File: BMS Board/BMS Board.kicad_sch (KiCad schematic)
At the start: 22 parts

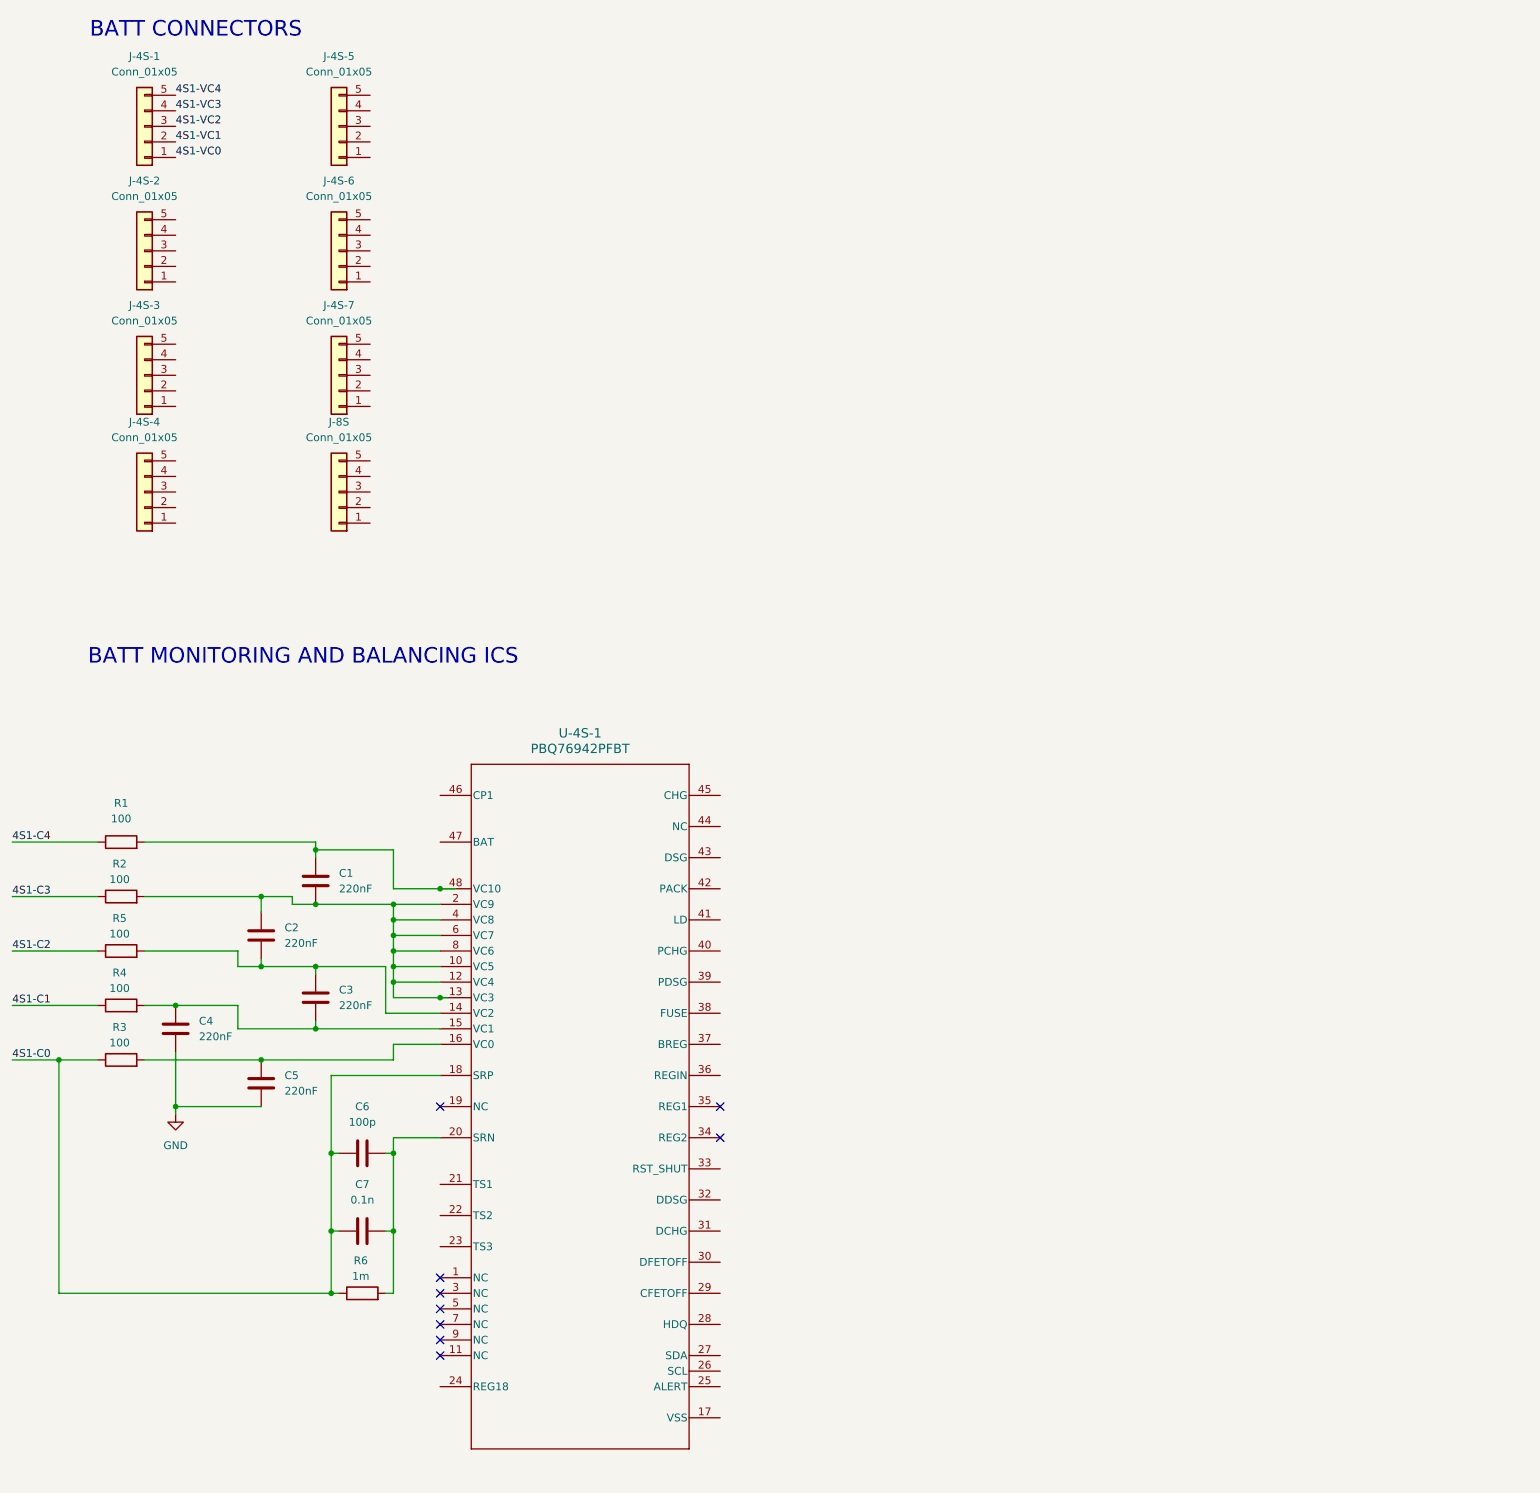
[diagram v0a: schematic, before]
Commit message: more pin configs for bq chip
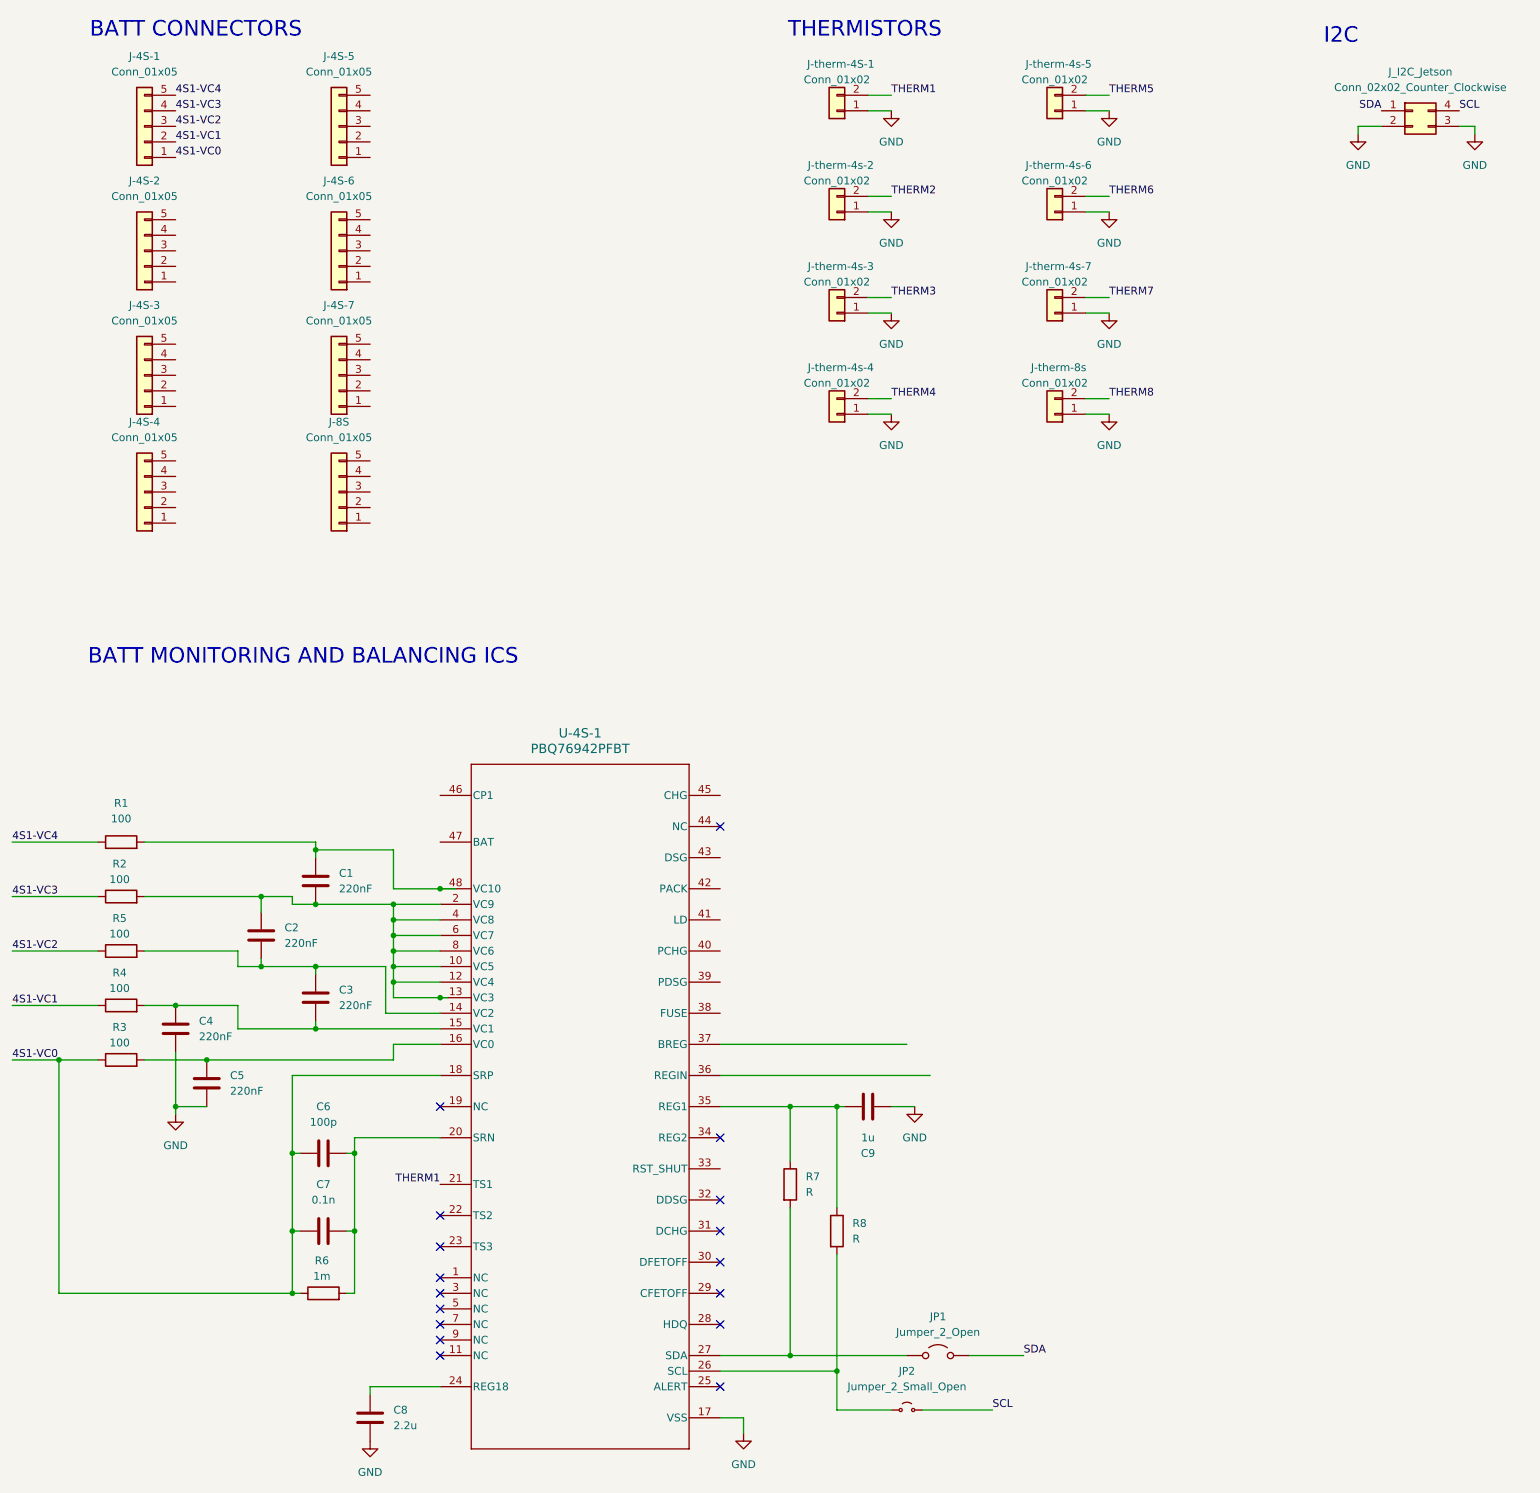
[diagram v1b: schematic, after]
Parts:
- added C8: 2.2u, symbol Device:C
- added C9: 1u, symbol Device:C
- added J-therm-4S-1, J-therm-4s-2, J-therm-4s-3, J-therm-4s-4, J-therm-4s-5, J-therm-4s-6, J-therm-4s-7, J-therm-8s: Conn_01x02, Connector_Molex:Molex_KK-254_AE-6410-02A_1x02_P2.54mm_Vertical, symbol Connector_Generic:Conn_01x02
- added JP1: Jumper_2_Open, symbol Jumper:Jumper_2_Open
- added JP2: Jumper_2_Small_Open, symbol Jumper:Jumper_2_Small_Open
- added J_I2C_Jetson: Conn_02x02_Counter_Clockwise, symbol Connector_Generic:Conn_02x02_Counter_Clockwise
- added R7, R8: R, symbol Device:R
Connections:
- net 4S1-C0 is gone; now on net 4S1-VC0: C6.1, C7.1, R3.1, R6.1, U-4S-1.18 (SRP)
- net 4S1-C1 is gone; now on net 4S1-VC1: R4.1
- net 4S1-C2 is gone; now on net 4S1-VC2: R5.1
- net 4S1-C3 is gone; now on net 4S1-VC3: R2.1
- net 4S1-C4 is gone; now on net 4S1-VC4: R1.1
- net GND: now also U-4S-1.17 (VSS), C8.2, C9.1, J-therm-4S-1.1 (Pin_1), J-therm-4s-2.1 (Pin_1), J-therm-4s-3.1 (Pin_1), J-therm-4s-4.1 (Pin_1), J-therm-4s-5.1 (Pin_1), J-therm-4s-6.1 (Pin_1), J-therm-4s-7.1 (Pin_1), J-therm-8s.1 (Pin_1), J_I2C_Jetson.2 (Pin_2), J_I2C_Jetson.3 (Pin_3)
- net THERM1: now reaches U-4S-1.21 (TS1)
- net THERM1: now also J-therm-4S-1.2 (Pin_2)
- net at U-4S-1.24 (REG18): now also C8.1
- net at U-4S-1.26 (SCL): now also JP2.1 (A), R8.2
- net at U-4S-1.27 (SDA): now also JP1.1 (A), R7.2
- net at U-4S-1.35 (REG1): now also C9.2, R7.1, R8.1
- new net SCL: JP2.2 (B), J_I2C_Jetson.4 (Pin_4)
- new net SDA: JP1.2 (B), J_I2C_Jetson.1 (Pin_1)
- new net THERM2: J-therm-4s-2.2 (Pin_2)
- new net THERM3: J-therm-4s-3.2 (Pin_2)
- new net THERM4: J-therm-4s-4.2 (Pin_2)
- new net THERM5: J-therm-4s-5.2 (Pin_2)
- new net THERM6: J-therm-4s-6.2 (Pin_2)
- new net THERM7: J-therm-4s-7.2 (Pin_2)
- new net THERM8: J-therm-8s.2 (Pin_2)
- no-connect marks 9 -> 17
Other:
- note added: "I2C"
- note added: "THERMISTORS"
- moved on the sheet: C5, C6, C7, R6

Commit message: BMS schematic with individual monitoring ICs + I2C MUX
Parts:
- removed JP1: Jumper_2_Open, symbol Jumper:Jumper_2_Open
- removed JP2: Jumper_2_Small_Open, symbol Jumper:Jumper_2_Small_Open
- removed U-4S-1: PBQ76942PFBT, PFB0048A_N, symbol Batt_Monitor:PBQ76942PFBT
- added C10, C11, C19, C20, C28, C29, C37, C38, C46, C47, C55, C56, C64, C66: 1uF, symbol Device:C
- added C12, C21, C30, C39, C48, C57, C65: 4.7uF, symbol Device:C
- added C13, C14, C15, C16, C17, C18, C22, C23, C24, C25, C26, C27, C31, C32, C33, C34, C35, C36, C40, C41, C42, C43, C44, C45, C49, C50, C51, C52, C53, C54, C58, C59, C60, C61, C62, C63, C67, C68, C69, C70, C71, C72, C73, C74, C75, C76, C77, C78: 220nF, symbol Device:C
- added D1, D2: D, symbol Device:D
- added J-8S1: Conn_01x05, symbol Connector_Generic:Conn_01x05
- added J-therm-8s1: Conn_01x02, Connector_Molex:Molex_KK-254_AE-6410-02A_1x02_P2.54mm_Vertical, symbol Connector_Generic:Conn_01x02
- added Q1: NMOS, symbol Simulation_SPICE:NMOS
- added R10, R18, R26, R34, R42, R50, R57, R9: 100k, symbol Device:R
- added R11, R12, R13, R14, R15, R16, R19, R20, R21, R22, R23, R24, R27, R28, R29, R30, R31, R32, R35, R36, R37, R38, R39, R40, R43, R44, R45, R46, R47, R48, R51, R52, R53, R54, R55, R56, R59, R60, R61, R62, R63, R64, R65, R66, R67, R68, R69, R70: 100, symbol Device:R
- added R17, R25, R33, R41, R49, R58: 10k, symbol Device:R
- added R71, R72, R73, R74, R75, R76, R77, R78, R79, R80, R81, R82, R83, R84, R85, R86, R87: 2.2k, symbol Device:R
- added U1, U3, U4, U5, U6, U7, U8: BQ76920PW, Package_SO:TSSOP-20_4.4x6.5mm_P0.65mm, symbol Battery_Management:BQ76920PW
- added U2: TCA9548APWR, Package_SO:TSSOP-24_4.4x7.8mm_P0.65mm, symbol Interface_Expansion:TCA9548APWR
- added U9: BQ76930DBT, Package_SO:TSSOP-30_4.4x7.8mm_P0.5mm, symbol Battery_Management:BQ76930DBT
- C6: value 100p -> 220nF
- C7: value 0.1n -> 4.7uF
- C8: value 2.2u -> 1uF
- C9: value 1u -> 1uF
- R6: value 1m -> 100
- R7, R8: value R -> 10k
- renumbered J-8S to J-8S0
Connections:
- net 4S1-VC0: now also R1.2; no longer C6.1, C7.1, R3.1, R6.1
- net 4S1-VC1: now also R2.2, R7.1; no longer R4.1
- net 4S1-VC2: now also R3.2; no longer R5.1
- net 4S1-VC3: now also R4.2; no longer R2.1
- net 4S1-VC4: now also C8.2, R5.2, R6.2, U1.9 (REGSRC); no longer R1.1
- net GND: now also C1.1, C2.2, C6.1, C7.1, C8.1, C9.2, C10.2, C11.1, C12.1, C13.1, C17.2, C18.1, C19.2, C20.1, C21.1, C22.1, C26.2, C27.1, C28.2, C29.1, C30.1, C31.1, C35.2, C36.1, C37.2, C38.1, C39.1, C40.1, C44.2, C45.1, C46.2, C47.1, C48.1, C49.1, C53.2, C54.1, C55.2, C56.1, C57.1, C58.1, C62.2, C63.1, C64.1, C65.1, C66.2, C70.2, C71.1, C78.1, R10.1, R18.1, R26.1, R34.1, R42.1, R50.1, R57.1, R9.1, U1.18 (SRP), U1.19 (SRN), U1.3 (VSS), U2.1 (A0), U2.12 (GND), U2.2 (A1), U2.21 (A2), U3.18 (SRP), U3.19 (SRN), U3.3 (VSS), U4.18 (SRP), U4.19 (SRN), U4.3 (VSS), U5.18 (SRP), U5.19 (SRN), U5.3 (VSS), U6.18 (SRP), U6.19 (SRN), U6.3 (VSS), U7.18 (SRP), U7.19 (SRN), U7.3 (VSS), U8.18 (SRP), U8.19 (SRN), U8.3 (VSS), U9.28 (SRP), U9.29 (SRN), U9.3 (VSS); no longer C4.2, C5.2, C8.2, C9.1
- net SCL: now also U2.22 (SCL)
- net SDA: now also U2.23 (SDA)
- net THERM1: now also R7.2, U1.6 (TS1)
- net THERM2: now also R8.2, U3.6 (TS1)
- net THERM3: now also R17.2, U4.6 (TS1)
- net THERM4: now also R25.2, U5.6 (TS1)
- net THERM5: now also R33.2, U6.6 (TS1)
- net THERM6: now also R41.2, U7.6 (TS1)
- net THERM7: now also R49.2, U8.6 (TS1)
- net 4S2-VC0: now reaches J-4S-2.1 (Pin_1)
- net 4S2-VC0: now also R16.2
- net 4S2-VC1: now reaches J-4S-2.2 (Pin_2)
- net 4S2-VC1: now also R8.1, R15.2
- net 4S2-VC2: now reaches J-4S-2.3 (Pin_3)
- net 4S2-VC2: now also R14.2
- net 4S2-VC3: now reaches J-4S-2.4 (Pin_4)
- net 4S2-VC3: now also R13.2
- net 4S2-VC4: now reaches J-4S-2.5 (Pin_5)
- net 4S2-VC4: now also C11.2, R11.2, R12.2, U3.9 (REGSRC)
- net 4S5-VC0: now reaches J-4S-5.1 (Pin_1)
- net 4S5-VC0: now also R40.2
- net 4S5-VC1: now reaches J-4S-5.2 (Pin_2)
- net 4S5-VC1: now also R33.1, R39.2
- net 4S5-VC2: now reaches J-4S-5.3 (Pin_3)
- net 4S5-VC2: now also R38.2
- net 4S5-VC3: now reaches J-4S-5.4 (Pin_4)
- net 4S5-VC3: now also R37.2
- net 4S5-VC4: now reaches J-4S-5.5 (Pin_5)
- net 4S5-VC4: now also C38.2, R35.2, R36.2, U6.9 (REGSRC)
- net at C5.1: now also R5.1, U1.12 (VC5); no longer R3.2
- net 4S6-VC0: now reaches J-4S-6.1 (Pin_1)
- net 4S6-VC0: now also R48.2
- net 4S6-VC1: now reaches J-4S-6.2 (Pin_2)
- net 4S6-VC1: now also R41.1, R47.2
- net 4S6-VC2: now reaches J-4S-6.3 (Pin_3)
- net 4S6-VC2: now also R46.2
- net 4S6-VC3: now reaches J-4S-6.4 (Pin_4)
- net 4S6-VC3: now also R45.2
- net 4S6-VC4: now reaches J-4S-6.5 (Pin_5)
- net 4S6-VC4: now also C47.2, R43.2, R44.2, U7.9 (REGSRC)
- net 4S7-VC0: now reaches J-4S-7.1 (Pin_1)
- net 4S7-VC0: now also R56.2
- net 4S7-VC1: now reaches J-4S-7.2 (Pin_2)
- net 4S7-VC1: now also R49.1, R55.2
- net 4S7-VC2: now reaches J-4S-7.3 (Pin_3)
- net 4S7-VC2: now also R54.2
- net 4S7-VC3: now reaches J-4S-7.4 (Pin_4)
- net 4S7-VC3: now also R53.2
- net 4S7-VC4: now reaches J-4S-7.5 (Pin_5)
- net 4S7-VC4: now also C56.2, R51.2, R52.2, U8.9 (REGSRC)
- net 4S3-VC0: now reaches J-4S-3.1 (Pin_1)
- net 4S3-VC0: now also R24.2
- net 4S3-VC1: now reaches J-4S-3.2 (Pin_2)
- net 4S3-VC1: now also R17.1, R23.2
- net 4S3-VC2: now reaches J-4S-3.3 (Pin_3)
- net 4S3-VC2: now also R22.2
- net 4S3-VC3: now reaches J-4S-3.4 (Pin_4)
- net 4S3-VC3: now also R21.2
- net 4S3-VC4: now reaches J-4S-3.5 (Pin_5)
- net 4S3-VC4: now also C20.2, R19.2, R20.2, U4.9 (REGSRC)
- net 4S4-VC0: now reaches J-4S-4.1 (Pin_1)
- net 4S4-VC0: now also R32.2
- net 4S4-VC1: now reaches J-4S-4.2 (Pin_2)
- net 4S4-VC1: now also R25.1, R31.2
- net 4S4-VC2: now reaches J-4S-4.3 (Pin_3)
- net 4S4-VC2: now also R30.2
- net 4S4-VC3: now reaches J-4S-4.4 (Pin_4)
- net 4S4-VC3: now also R29.2
- net 4S4-VC4: now reaches J-4S-4.5 (Pin_5)
- net 4S4-VC4: now also C29.2, R27.2, R28.2, U5.9 (REGSRC)
- net THERM8 renamed THERM8_1
- net THERM8_1: now also R58.2, U9.6 (TS1)
- new net: C14.1, R12.1, U3.12 (VC5)
- new net: C14.2, C15.1, R13.1, U3.13 (VC4), U3.14 (VC3)
- new net: C31.2, R27.1, U5.10 (BAT)
- new net: C32.1, R28.1, U5.12 (VC5)
- new net: C32.2, C33.1, R29.1, U5.13 (VC4), U5.14 (VC3)
- new net: C33.2, C34.1, R30.1, U5.15 (VC2)
- new net: C34.2, C35.1, R31.1, U5.16 (VC1)
- new net: C36.2, R32.1, U5.17 (VC0)
- new net: R26.2, U5.20 (ALERT)
- new net: C28.1, U5.7 (CAP1)
- new net: C30.2, U5.8 (REGOUT)
- new net: C48.2, U7.8 (REGOUT)
- new net: R57.2, U9.30 (ALERT)
- new net: C23.2, C24.1, R21.1, U4.13 (VC4), U4.14 (VC3)
- new net: C39.2, U6.8 (REGOUT)
- new net: C23.1, R20.1, U4.12 (VC5)
- new net: C6.2, R6.1, U1.10 (BAT)
- new net: C59.1, R52.1, U8.12 (VC5)
- new net: C59.2, C60.1, R53.1, U8.13 (VC4), U8.14 (VC3)
- new net: C65.2, U9.8 (REGOUT)
- new net: C77.2, D1.1 (K), R70.1, U9.15 (BAT)
- new net: C76.1, D1.2 (A), R68.1, U9.16 (VC10)
- new net: C1.2, R1.1, U1.17 (VC0)
- new net: C15.2, C16.1, R14.1, U3.15 (VC2)
- new net: C60.2, C61.1, R54.1, U8.15 (VC2)
- new net: C61.2, C62.1, R55.1, U8.16 (VC1)
- new net: C27.2, R24.1, U4.17 (VC0)
- new net: C22.2, R19.1, U4.10 (BAT)
- new net: C67.1, D2.2 (A), R59.1, U9.22 (VC5)
- new net: C72.1, C74.2, R65.1, U9.20 (VC6)
- new net: C64.2, Q1.3 (S), U9.9 (REGSRC)
- new net: C42.2, C43.1, R38.1, U6.15 (VC2)
- new net: C73.2, R66.1, U9.21 (VC5B)
- new net: C16.2, C17.1, R15.1, U3.16 (VC1)
- new net: C75.1, C76.2, R67.1, U9.17 (VC9), U9.18 (VC8)
- new net: C63.2, R56.1, U8.17 (VC0)
- new net: R10.2, U3.20 (ALERT)
- new net: C57.2, U8.8 (REGOUT)
- new net: C68.2, C69.1, R61.1, U9.25 (VC2)
- new net: C69.2, C70.1, R62.1, U9.26 (VC1)
- new net: C2.1, C3.2, R2.1, U1.16 (VC1)
- new net: C45.2, R40.1, U6.17 (VC0)
- new net: C40.2, R35.1, U6.10 (BAT)
- new net: C71.2, R63.1, U9.27 (VC0)
- new net: C50.1, R44.1, U7.12 (VC5)
- new net: C43.2, C44.1, R39.1, U6.16 (VC1)
- new net: R87.2, U2.3 (~{RESET})
- new net: C24.2, C25.1, R22.1, U4.15 (VC2)
- new net: C67.2, C68.1, R60.1, U9.23 (VC4), U9.24 (VC3)
- new net: C41.1, R36.1, U6.12 (VC5)
- new net: C41.2, C42.1, R37.1, U6.13 (VC4), U6.14 (VC3)
- new net: C7.2, U1.8 (REGOUT)
- new net: C13.2, R11.1, U3.10 (BAT)
- new net: C4.1, C5.2, R4.1, U1.13 (VC4), U1.14 (VC3)
- new net: C3.1, C4.2, R3.1, U1.15 (VC2)
- new net: C74.1, C75.2, R69.1, U9.19 (VC7)
- new net: C37.1, U6.7 (CAP1)
- new net: U9.11 (NC(CAP2)), U9.12 (NC(CAP2)), U9.14 (CAP2)
- new net: C66.1, U9.7 (CAP1)
- new net: C49.2, R43.1, U7.10 (BAT)
- new net: R34.2, U6.20 (ALERT)
- new net: C50.2, C51.1, R45.1, U7.13 (VC4), U7.14 (VC3)
- new net: C18.2, R16.1, U3.17 (VC0)
- new net: C52.2, C53.1, R47.1, U7.16 (VC1)
- new net: C25.2, C26.1, R23.1, U4.16 (VC1)
- new net: C58.2, R51.1, U8.10 (BAT)
- new net: R50.2, U8.20 (ALERT)
- new net: C55.1, U8.7 (CAP1)
- new net: R18.2, U4.20 (ALERT)
- new net: C19.1, U4.7 (CAP1)
- new net: C21.2, U4.8 (REGOUT)
- new net: C10.1, U3.7 (CAP1)
- new net: C12.2, U3.8 (REGOUT)
- new net: C9.1, U1.7 (CAP1)
- new net: C51.2, C52.1, R46.1, U7.15 (VC2)
- new net: C54.2, R48.1, U7.17 (VC0)
- new net: R42.2, U7.20 (ALERT)
- new net: C46.1, U7.7 (CAP1)
- new net: R9.2, U1.20 (ALERT)
- new net 3.3V: R71.1, R72.1, R73.1, R74.1, R75.1, R76.1, R77.1, R78.1, R79.2, R80.2, R81.2, R82.2, R83.2, R84.2, R85.2, R86.2, R87.1, U2.24 (VCC)
- new net 8S-VC0: R63.2
- new net 8S-VC1: R58.1, R62.2
- new net 8S-VC2: R61.2
- new net 8S-VC3: R60.2
- new net 8S-VC4: R59.2, R64.1, R66.2
- new net 8S-VC6: R65.2
- new net 8S-VC7: R69.2
- new net 8S-VC8: R67.2
- new net 8S-VC9: Q1.1 (D), R68.2, R70.2
- new net SC0: R71.2, U1.5 (SCL), U2.5 (SC0)
- new net SC1: R73.2, U2.7 (SC1), U3.5 (SCL)
- new net SC2: R75.2, U2.9 (SC2), U4.5 (SCL)
- new net SC3: R77.2, U2.11 (SC3), U5.5 (SCL)
- new net SC4: R79.1, U2.14 (SC4), U6.5 (SCL)
- new net SC5: R81.1, U2.16 (SC5), U7.5 (SCL)
- new net SC6: R83.1, U2.18 (SC6), U8.5 (SCL)
- new net SC7: R84.1, U2.20 (SC7), U9.5 (SCL)
- new net SD0: R72.2, U1.4 (SDA), U2.4 (SD0)
- new net SD1: R74.2, U2.6 (SD1), U3.4 (SDA)
- new net SD2: R76.2, U2.8 (SD2), U4.4 (SDA)
- new net SD3: R78.2, U2.10 (SD3), U5.4 (SDA)
- new net SD4: R80.1, U2.13 (SD4), U6.4 (SDA)
- new net SD5: R82.1, U2.15 (SD5), U7.4 (SDA)
- new net SD6: R85.1, U2.17 (SD6), U8.4 (SDA)
- new net SD7: R86.1, U2.19 (SD7), U9.4 (SDA)
- new net THERM8_2: J-therm-8s1.2 (Pin_2), U9.13 (TS2)
- new net VC5X: C72.2, C73.1, C77.1, C78.2, D2.1 (K), J-therm-8s1.1 (Pin_1), Q1.2 (G), R64.2, U9.10 (VC5X)
- no-connect marks 17 -> 16
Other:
- note added: "0x18 I2C for each: need multiplexer"
- note added: "BATT CONNECTORS - recheck their orientation depending on the actual JST-XH connectors"
- note added: "BQ7692006PWR 0x18 I2C for each"
- note added: "BQ7693006DBT Need to figure out which NMOS to use Recheck Cf and Rf values"
- note added: "MULTIPLEXER - hex address 70"
- note added: "Need two of these since 2 4S in series Use different batt monitor IC with 8 inputs here"
- note removed: "BATT CONNECTORS"
- moved on the sheet: C1, J-4S-4, J-8S0, R1

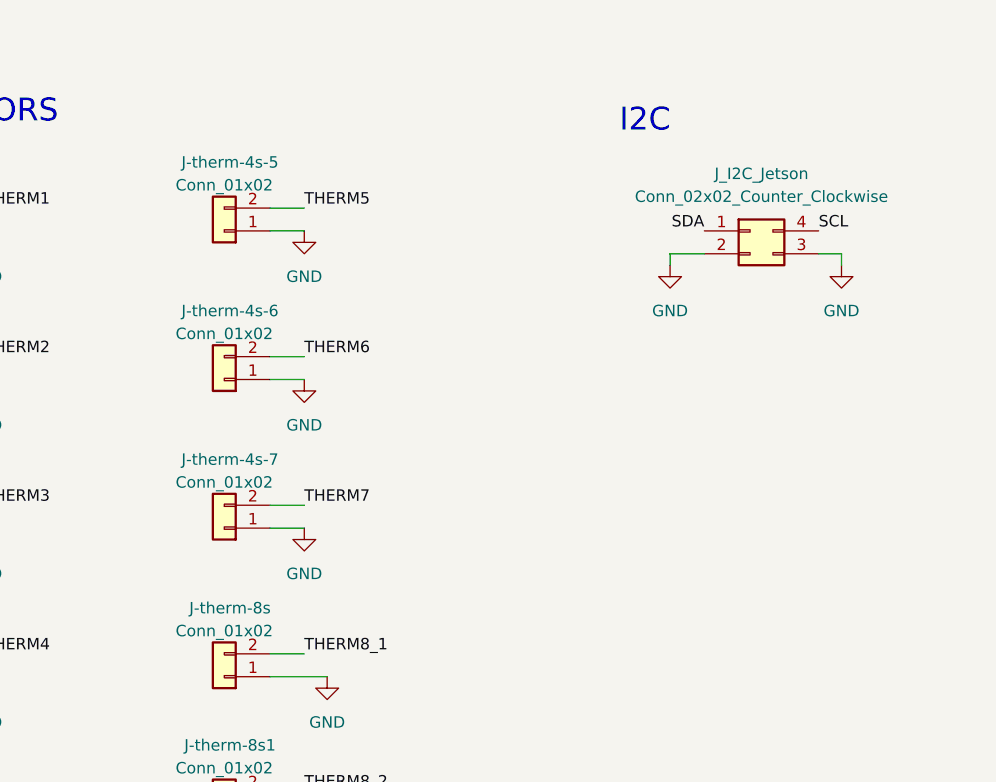
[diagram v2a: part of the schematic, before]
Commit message: started pcb layout for BMS board
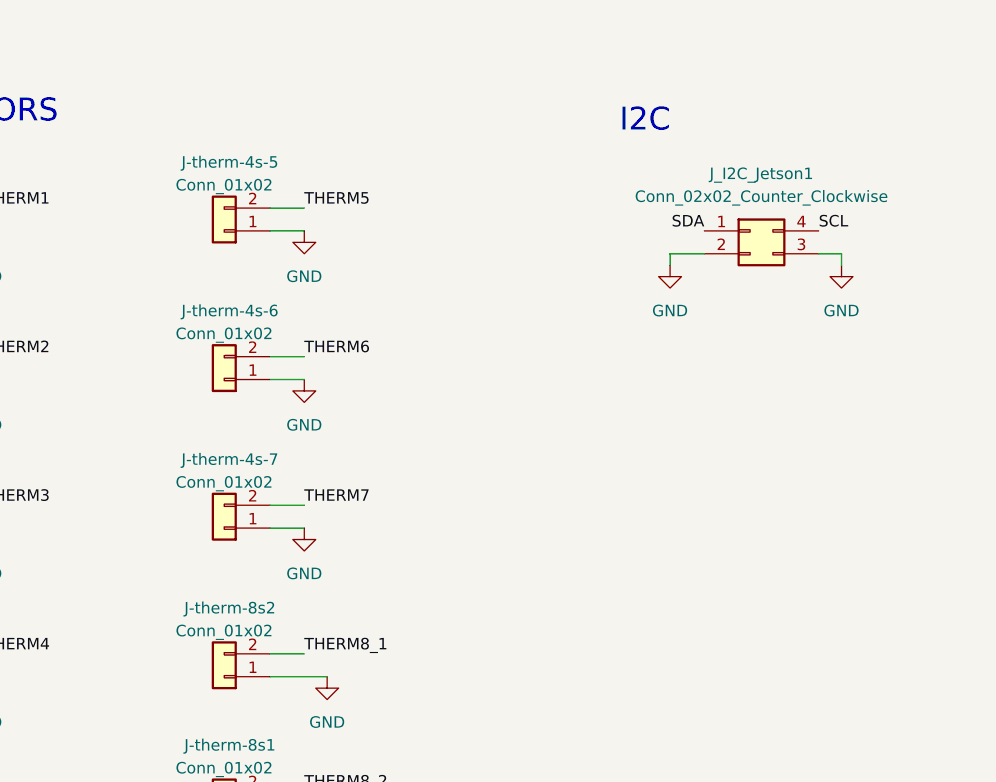
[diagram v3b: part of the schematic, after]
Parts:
- C1, C10, C11, C12, C13, C14, C15, C16, C17, C18, C19, C2, C20, C21, C22, C23, C24, C25, C26, C27, C28, C29, C3, C30, C31, C32, C33, C34, C35, C36, C37, C38, C39, C4, C40, C41, C42, C43, C44, C45, C46, C47, C48, C49, C5, C50, C51, C52, C53, C54, C55, C56, C57, C58, C59, C6, C60, C61, C62, C63, C64, C65, C66, C67, C68, C69, C7, C70, C71, C72, C73, C74, C75, C76, C77, C78, C8, C9, R1, R10, R11, R12, R13, R14, R15, R16, R17, R18, R19, R2, R20, R21, R22, R23, R24, R25, R26, R27, R28, R29, R3, R30, R31, R32, R33, R34, R35, R36, R37, R38, R39, R4, R40, R41, R42, R43, R44, R45, R46, R47, R48, R49, R5, R50, R51, R52, R53, R54, R55, R56, R57, R58, R59, R6, R60, R61, R62, R63, R64, R65, R66, R67, R68, R69, R7, R70, R71, R72, R73, R74, R75, R76, R77, R78, R79, R8, R80, R81, R82, R83, R84, R85, R86, R87, R9: footprint (none) -> Capacitor_SMD:C_0603_1608Metric
- J-4S-1, J-4S-2, J-4S-3, J-4S-4, J-4S-5, J-4S-6, J-4S-7, J-8S0, J-8S1: footprint (none) -> Connector_JST:JST_XH_B5B-XH-A_1x05_P2.50mm_Vertical
- renumbered J-therm-8s to J-therm-8s2, J_I2C_Jetson to J_I2C_Jetson1
